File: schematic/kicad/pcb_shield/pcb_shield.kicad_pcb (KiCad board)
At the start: 2 copper layers, 70 x 57.5 mm, 9 parts, among them U2 NUCLEO-F411RE

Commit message: change shield template1
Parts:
- removed U2: NUCLEO-F411RE, NUCLEO-F411RE:BOARD_NUCLEO-F411RE_custom
- added H1: MountingHole, MountingHole:MountingHole_3.2mm_M3, F.Cu at (145.4, 110.4)
- added H2: MountingHole, MountingHole:MountingHole_3.2mm_M3, F.Cu at (112.4, 58.4)
- added H3: MountingHole, MountingHole:MountingHole_3.2mm_M3, F.Cu at (160.6, 59.7)
- added J1: CN7, Connector_PinSocket_2.54mm:PinSocket_2x19_P2.54mm_Vertical, B.Cu at (104.8, 62.2)
- added J2: CN10, Connector_PinSocket_2.54mm:PinSocket_2x19_P2.54mm_Vertical, B.Cu at (165.7, 62.2)
- moved BL_E1 36.2 mm to (129.5, 88.0)
- moved BR_E1 36.2 mm to (134.2, 88.0)
- moved BR_M1 34.1 mm to (134.2, 78.3)
- moved BL_M1 34.1 mm to (129.5, 78.3)
- moved FL_E1 28.0 mm to (138.8, 88.0)
- moved FR_E1 28.0 mm to (143.5, 88.0)
- moved FL_M1 25.5 mm to (138.8, 78.3)
- moved FR_M1 25.5 mm to (143.5, 78.3)
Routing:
- net GND: track 0.00 -> 96.8 mm
- net +5V: track 0.00 -> 39.5 mm
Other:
- board text removed: "+5V"
- board text removed: "A"
- board text removed: "B"
- board text removed: "EN"
- board text removed: "GND"

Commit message: first working versio
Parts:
- added PWR1: POWER, Connector_PinHeader_2.54mm:PinHeader_1x03_P2.54mm_Vertical, F.Cu at (134.0, 101.6)
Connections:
- J1 pad 24: /VIN -> +12V
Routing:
- net GND: track 96.8 -> 0.00 mm
- net FR_MOTOR_A: track 0.00 -> 58.0 mm
- net FR_MOTOR_B: track 0.00 -> 56.0 mm
- net BL_MOTOR_EN: track 0.00 -> 49.8 mm
- net FL_MOTOR_A: track 0.00 -> 49.6 mm
- net FL_MOTOR_B: track 0.00 -> 44.7 mm
- net BL_MOTOR_A: track 0.00 -> 44.6 mm
- net BL_ENCODER_A: track 0.00 -> 43.7 mm
- net BR_MOTOR_B: track 0.00 -> 37.8 mm
- net +12V: track 0.00 -> 36.8 mm, vias 0 -> 1
- net FL_MOTOR_EN: track 0.00 -> 36.5 mm
- net BR_MOTOR_EN: track 0.00 -> 35.6 mm
- net BR_MOTOR_A: track 0.00 -> 35.6 mm
- net FL_ENCODER_A: track 0.00 -> 34.4 mm
- net BL_MOTOR_B: track 0.00 -> 33.8 mm
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- added copper zone on In1.Cu, net GND
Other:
- copper layers 2 -> 4

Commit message: first actual working version
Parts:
- added CTRL_UART1: CTRL_UART, Connector_PinHeader_2.54mm:PinHeader_1x04_P2.54mm_Vertical, F.Cu at (140.3, 70.8)
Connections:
- J2 pad 19: /PC7 -> RX6
- J2 pad 4: /PC6 -> TX6
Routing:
- net GND: track 0.00 -> 136.9 mm
- net RX6: track 0.00 -> 52.6 mm
- net TX6: track 0.00 -> 35.5 mm
- net +5V: track 50.5 -> 71.1 mm
- net FR_MOTOR_A: track 58.0 -> 76.6 mm
- net FL_MOTOR_A: track 49.6 -> 62.7 mm, vias 0 -> 1
- net BL_MOTOR_EN: track 49.8 -> 59.0 mm
- net FL_MOTOR_B: track 44.7 -> 53.6 mm
- net BL_ENCODER_A: track 43.7 -> 52.2 mm, vias 0 -> 1
- net FR_ENCODER_B: track 28.7 -> 36.7 mm
- net FL_MOTOR_EN: track 36.5 -> 31.8 mm
- net FL_ENCODER_A: track 34.4 -> 38.9 mm, vias 0 -> 1
- net FR_MOTOR_B: track 56.0 -> 59.8 mm
- net BL_MOTOR_A: track 44.6 -> 47.9 mm
- net +12V: track 36.8 -> 39.6 mm, vias 1 -> 0
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- removed copper zone on In1.Cu, net GND
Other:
- copper layers 4 -> 2
- board text added: "+5V"
- board text added: "5V"
- board text added: "A"
- board text added: "B"
- board text added: "EN"
- board text added: "G"
- board text added: "GND"
- board text added: "RX"
- board text added: "TX"

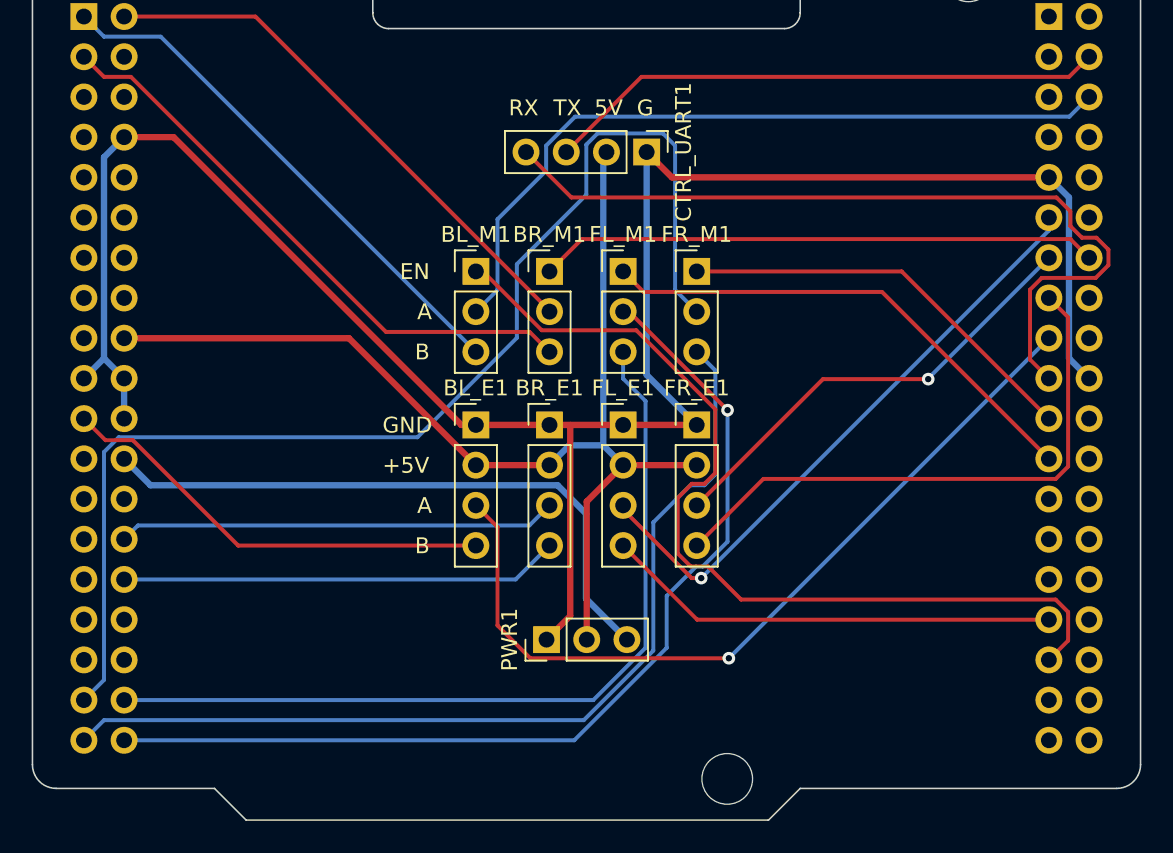
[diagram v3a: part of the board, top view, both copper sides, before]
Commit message: fix power input connector
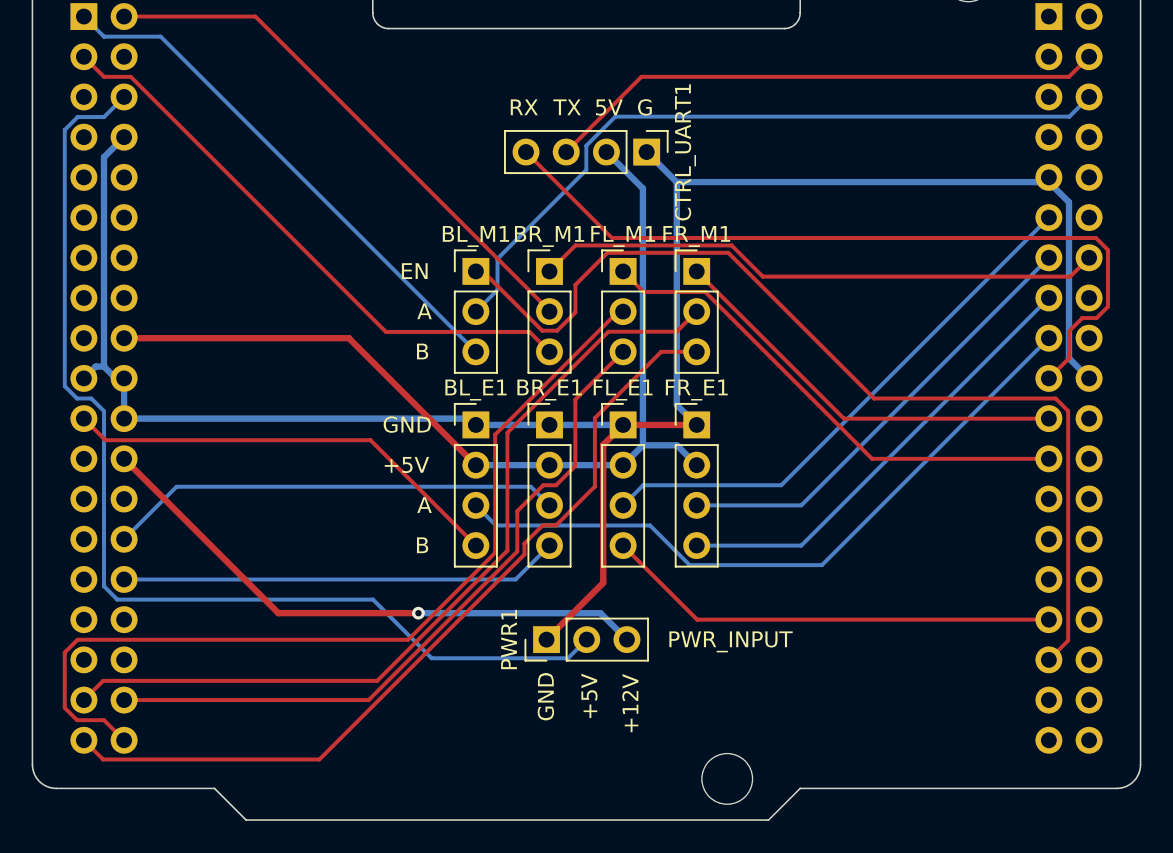
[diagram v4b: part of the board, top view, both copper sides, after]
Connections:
- PWR1 pad 2: +5V -> /E5V
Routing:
- net /E5V: track 0.00 -> 67.9 mm
- net FR_MOTOR_A: track 76.6 -> 53.2 mm
- net +5V: track 71.1 -> 60.0 mm
- net FL_MOTOR_B: track 53.6 -> 44.6 mm
- net BL_ENCODER_A: track 52.2 -> 43.7 mm, vias 1 -> 0
- net GND: track 136.9 -> 128.4 mm
- net FR_ENCODER_B: track 36.7 -> 28.7 mm
- net FR_MOTOR_B: track 59.8 -> 52.8 mm
- net FL_MOTOR_A: track 62.7 -> 56.7 mm, vias 1 -> 0
- net FL_ENCODER_A: track 38.9 -> 34.4 mm, vias 1 -> 0
- net BL_MOTOR_EN: track 59.0 -> 62.4 mm
- net +12V: track 39.6 -> 36.5 mm, vias 0 -> 1
- net RX6: track 52.6 -> 49.5 mm
- net BL_MOTOR_A: track 47.9 -> 46.4 mm
- net BR_ENCODER_A: track 27.8 -> 28.7 mm
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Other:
- board text added: "+12V"
- board text added: "PWR_INPUT"
